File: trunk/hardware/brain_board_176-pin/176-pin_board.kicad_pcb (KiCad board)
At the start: 4 copper layers, 61.8 x 73.2 mm, 75 parts, among them J1 MINI-USB-5P-3400020P1, P1 CONN_25X2, P10 CONN_2X2, P11 CONN_4X2, P12 CONN_4X2, P2 CONN_25X2, P3 CONN_2, P4 CONN_6, P5 CONN_1, P6 CONN_2X2, P7 CONN_4X2, P8 CONN_4X2, P9 CONN_4X2, SW1 SW_PUSH, U1 STM32F407IGT6, U2 NUF2101MT1G, U3 LM2937, X1 CRYSTAL, X2 CRYSTAL

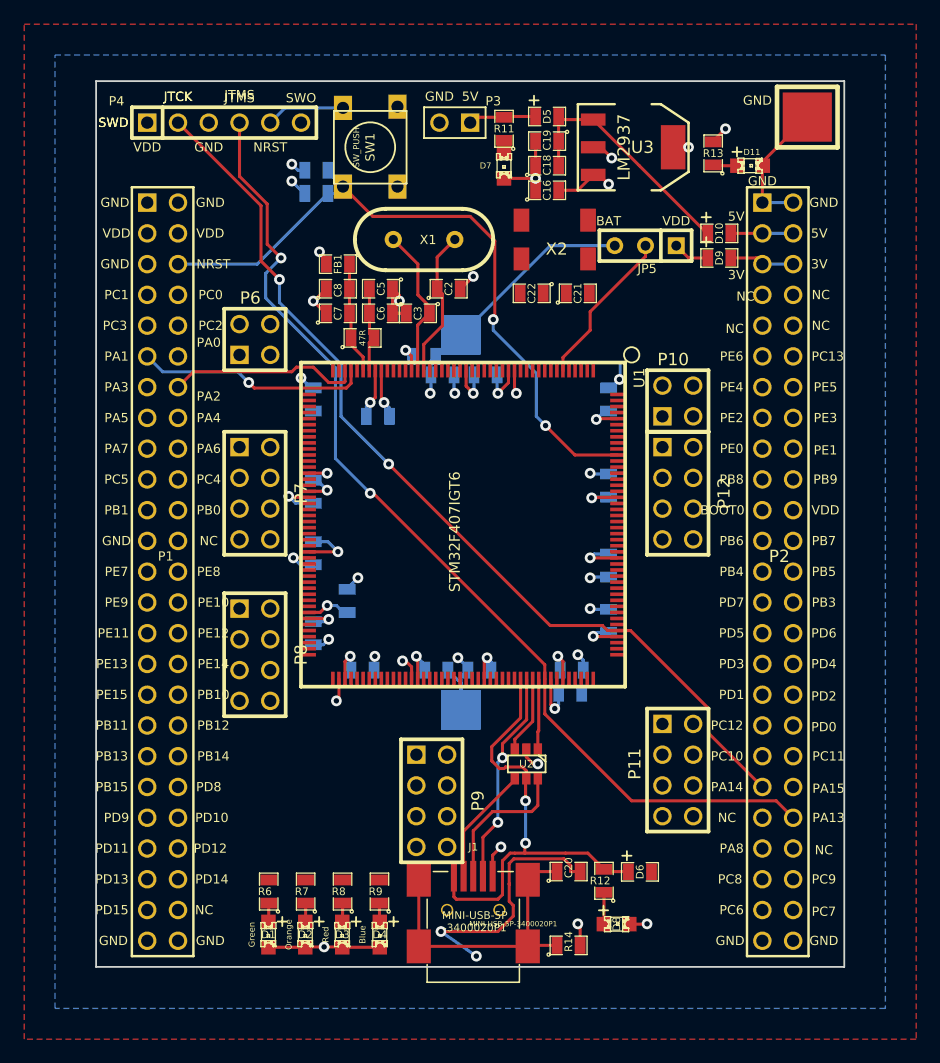
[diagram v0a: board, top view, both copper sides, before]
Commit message: 
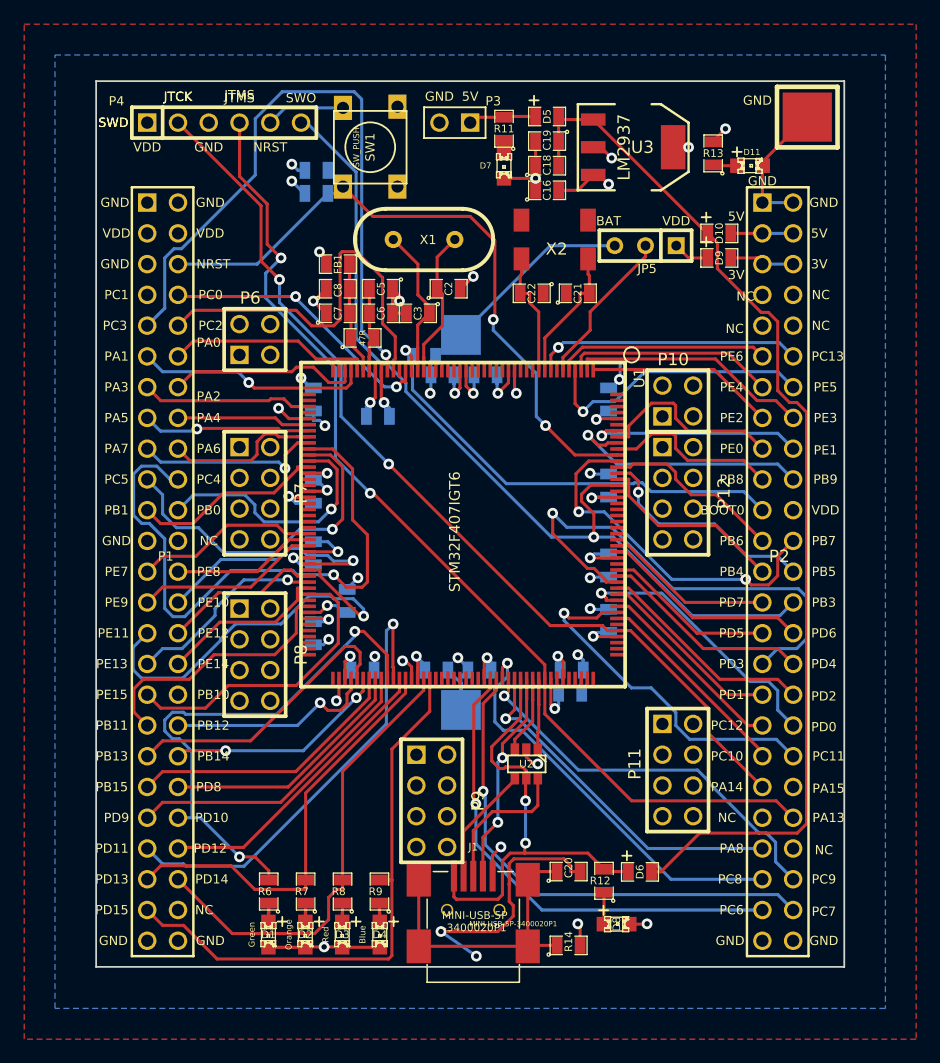
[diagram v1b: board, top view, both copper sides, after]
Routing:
- net /PB3: track 0.00 -> 73.6 mm, vias 0 -> 1
- net /5Vi: track 20.4 -> 88.7 mm
- net /PC3: track 0.00 -> 54.4 mm, vias 0 -> 1
- net /PC4: track 0.00 -> 50.4 mm, vias 0 -> 1
- net /PD15: track 0.00 -> 47.2 mm
- net /PD10: track 0.00 -> 44.0 mm, vias 0 -> 2
- net /PC7: track 0.00 -> 41.9 mm, vias 0 -> 1
- net /PD3: track 0.00 -> 40.6 mm, vias 0 -> 1
- net /PC6: track 0.00 -> 40.2 mm, vias 0 -> 1
- net /PD11: track 0.00 -> 38.3 mm, vias 0 -> 1
- net /PD14: track 0.00 -> 38.2 mm
- net /BOOT0: track 2.64 -> 39.1 mm
- net /PD13: track 0.00 -> 35.1 mm
- net /PC8: track 0.00 -> 34.2 mm, vias 0 -> 1
- net /PE11: track 0.00 -> 33.1 mm, vias 0 -> 1
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
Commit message: 
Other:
- net class Default: clearance 0.2032 -> 0.1524; trace_width 0.254 -> 0.1524
- rule trace_clearance: 0.2032 -> 0.1524
- rule trace_min: 0.254 -> 0.1524
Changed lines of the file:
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@@
   (general
     (links 250)
-    (no_connects 81)
+    (no_connects 8)
     (area 65.982549 61.494999 160.020001 171.672001)
     (thickness 1.6)
@@
   )
   (setup
-    (last_trace_width 0.254)
-    (trace_clearance 0.2032)
+    (last_trace_width 0.1524)
+    (trace_clearance 0.1524)
     (zone_clearance 0.254)
     (zone_45_only no)
-    (trace_min 0.254)
+    (trace_min 0.1524)
     (segment_width 0.2)
     (edge_width 0.15)
@@
   (net 105 N-0000078)
   (net_class Default "Это класс цепей по умолчанию."
-    (clearance 0.2032)
-    (trace_width 0.254)
+    (clearance 0.1524)
+    (trace_width 0.1524)
     (via_dia 0.889)
     (via_drill 0.635)

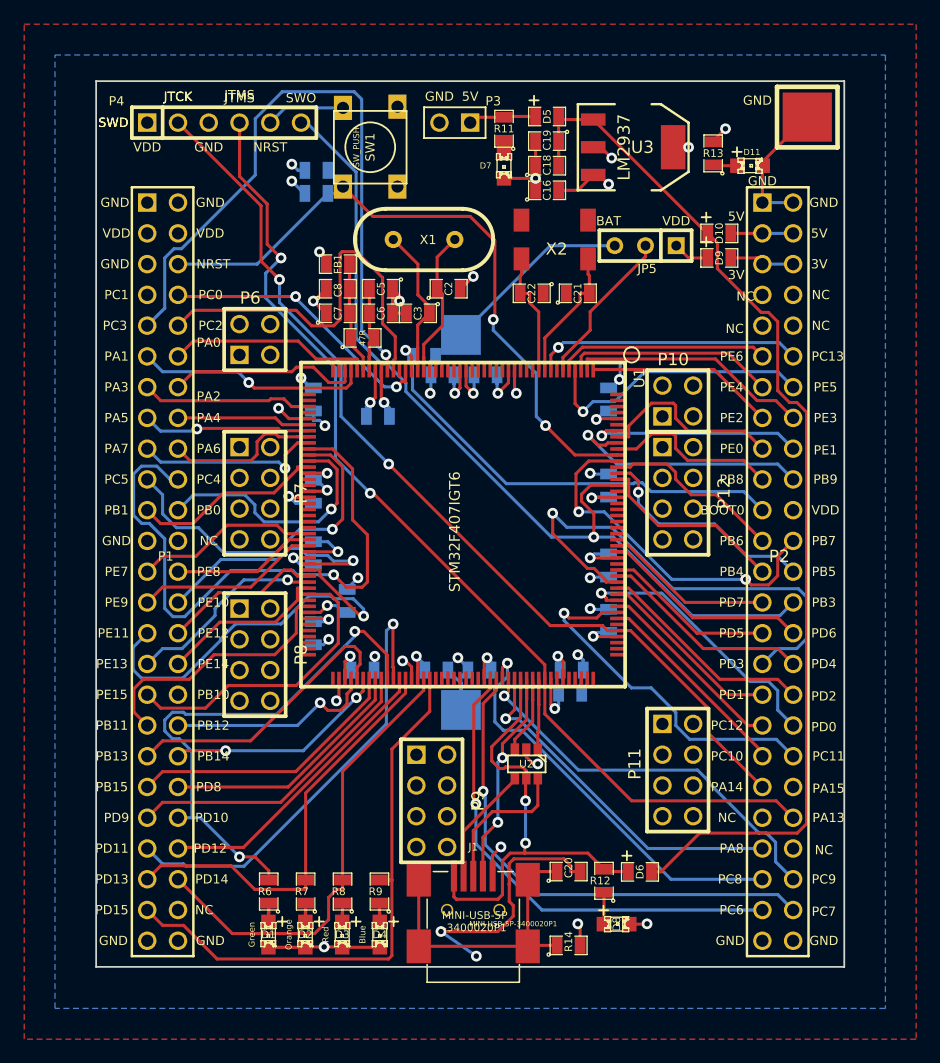
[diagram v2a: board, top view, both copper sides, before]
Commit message: 
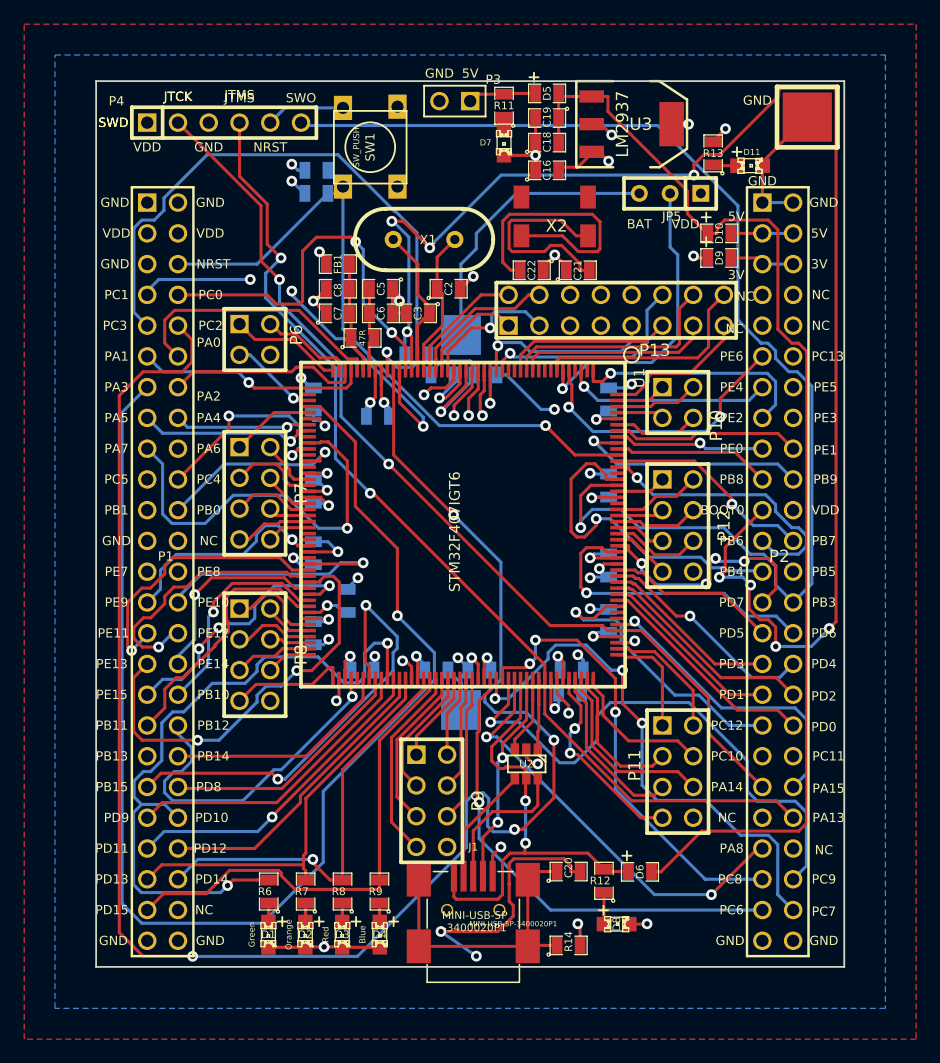
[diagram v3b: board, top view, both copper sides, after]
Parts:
- added P13: CONN_8X2, pin_array_8x2, F.Cu at (130.2, 102.4)
- moved JP5 4.77 mm to (134.6, 92.7)
- moved P12 2.67 mm to (135.3, 120.1)
- moved U3 1.91 mm to (131.4, 87.0)
- moved C18 1.91 mm to (124.5, 88.5)
- moved C19 1.91 mm to (124.5, 86.5)
- moved C21 1.91 mm to (127.0, 99.1)
- moved C22 1.91 mm to (123.2, 99.1)
- moved D5 1.91 mm to (124.5, 84.5)
- moved D7 1.91 mm to (120.9, 88.5)
- moved R11 1.91 mm to (120.9, 85.5)
- moved X2 1.91 mm to (125.1, 94.6)
- moved P3 1.78 mm to (116.8, 85.1)
- moved C16 1.65 mm to (124.5, 90.8)
- moved R4 0.65 mm to (113.7, 106.0)
- moved P10 0.13 mm to (135.3, 110.0), turned to 270 degrees
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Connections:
- P10 pad 1: (no net) -> /PI6
- P10 pad 2: (no net) -> /PI5
- P10 pad 3: (no net) -> /PI4
- P10 pad 4: (no net) -> /PDR_ON
- P11 pad 1: (no net) -> /PI2
- P11 pad 2: (no net) -> /PI3
- P11 pad 3: (no net) -> /PI0
- P11 pad 4: (no net) -> /PI1
- P11 pad 5: (no net) -> /PH14
- P11 pad 6: (no net) -> /PH15
- P11 pad 7: (no net) -> /PH13
- P11 pad 8: (no net) -> GND
- P12 pad 1: (no net) -> /PG15
- P12 pad 2: (no net) -> /PG14
- P12 pad 3: (no net) -> /PG13
- P12 pad 4: (no net) -> /PG12
- P12 pad 5: (no net) -> /PG11
- P12 pad 6: (no net) -> /PG10
- P12 pad 7: (no net) -> /PG9
- P12 pad 8: (no net) -> GND
- P6 pad 1: (no net) -> /PH3
- P6 pad 2: (no net) -> /PH2
- P6 pad 3: (no net) -> /PH5
- P6 pad 4: (no net) -> /PH4
- P7 pad 1: (no net) -> /BYPASS_REG
- P7 pad 2: (no net) -> /PF11
- P7 pad 3: (no net) -> /PF12
- P7 pad 4: (no net) -> /PF13
- P7 pad 5: (no net) -> /PF14
- P7 pad 6: (no net) -> /PF15
- P7 pad 7: (no net) -> /PG0
- P7 pad 8: (no net) -> /PG1
- P8 pad 1: (no net) -> /PH6
- P8 pad 2: (no net) -> /PH7
- P8 pad 3: (no net) -> /PH8
- P8 pad 4: (no net) -> /PH9
- P8 pad 5: (no net) -> /PH10
- P8 pad 6: (no net) -> /PH11
- P8 pad 7: (no net) -> /PH12
- P8 pad 8: (no net) -> GND
- P9 pad 1: (no net) -> /PG5
- P9 pad 2: (no net) -> /PG6
- P9 pad 3: (no net) -> /PG4
- P9 pad 4: (no net) -> /PG7
- P9 pad 5: (no net) -> /PG3
- P9 pad 6: (no net) -> /PG8
- P9 pad 7: (no net) -> /PG2
- P9 pad 8: (no net) -> GND
- U1 pad 106: (no net) -> /PG2
- U1 pad 107: (no net) -> /PG3
- U1 pad 108: (no net) -> /PG4
- U1 pad 109: (no net) -> /PG5
- U1 pad 11: (no net) -> /PI9
- U1 pad 110: (no net) -> /PG6
- U1 pad 111: (no net) -> /PG7
- U1 pad 112: (no net) -> /PG8
- U1 pad 12: (no net) -> /PI10
- U1 pad 128: (no net) -> /PH13
- U1 pad 129: (no net) -> /PH14
- U1 pad 13: (no net) -> /PI11
- U1 pad 130: (no net) -> /PH15
- U1 pad 131: (no net) -> /PI0
- U1 pad 132: (no net) -> /PI1
- U1 pad 133: (no net) -> /PI2
- U1 pad 134: (no net) -> /PI3
- U1 pad 152: (no net) -> /PG9
- U1 pad 153: (no net) -> /PG10
- U1 pad 154: (no net) -> /PG11
- U1 pad 155: (no net) -> /PG12
- U1 pad 156: (no net) -> /PG13
- U1 pad 157: (no net) -> /PG14
- U1 pad 16: (no net) -> /PF0
- U1 pad 160: (no net) -> /PG15
- U1 pad 17: (no net) -> /PF1
- U1 pad 171: (no net) -> /PDR_ON
- U1 pad 173: (no net) -> /PI4
- U1 pad 174: (no net) -> /PI5
- U1 pad 175: (no net) -> /PI6
- U1 pad 176: (no net) -> /PI7
- U1 pad 18: (no net) -> /PF2
- U1 pad 19: (no net) -> /PF3
- U1 pad 20: (no net) -> /PF4
- U1 pad 21: (no net) -> /PF5
- U1 pad 24: (no net) -> /PF6
- U1 pad 25: (no net) -> /PF7
- U1 pad 26: (no net) -> /PF8
- U1 pad 27: (no net) -> /PF9
- U1 pad 28: (no net) -> /PF10
- U1 pad 43: (no net) -> /PH2
- U1 pad 44: (no net) -> /PH3
- U1 pad 45: (no net) -> /PH4
- U1 pad 46: (no net) -> /PH5
- U1 pad 48: (no net) -> /BYPASS_REG
- U1 pad 59: (no net) -> /PF11
- U1 pad 60: (no net) -> /PF12
- U1 pad 63: (no net) -> /PF13
- U1 pad 64: (no net) -> /PF14
- U1 pad 65: (no net) -> /PF15
- U1 pad 66: (no net) -> /PG0
- U1 pad 67: (no net) -> /PG1
- U1 pad 7: (no net) -> /PI8
- U1 pad 83: (no net) -> /PH6
- U1 pad 84: (no net) -> /PH7
- U1 pad 85: (no net) -> /PH8
- U1 pad 86: (no net) -> /PH9
- U1 pad 87: (no net) -> /PH10
- U1 pad 88: (no net) -> /PH11
- U1 pad 89: (no net) -> /PH12
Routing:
- net /PC2: track 32.7 -> 146.9 mm, vias 0 -> 4
- net /PA3: track 14.1 -> 109.2 mm, vias 0 -> 1
- net /BOOT0: track 39.1 -> 125.8 mm, vias 1 -> 8
- net /PC1: track 0.00 -> 35.9 mm, vias 0 -> 3
- net /PC4: track 50.4 -> 17.5 mm, vias 1 -> 2
- net /PB3: track 73.6 -> 104.2 mm
- net /PF6: track 0.00 -> 29.6 mm, vias 0 -> 1
- net /PC11: track 29.6 -> 0.00 mm, vias 1 -> 0
- net /PC5: track 28.2 -> 0.00 mm, vias 1 -> 0
- net /PD3: track 40.6 -> 14.8 mm, vias 1 -> 0
- net /PA15: track 0.00 -> 25.2 mm, vias 0 -> 1
- net /PB13: track 23.8 -> 0.00 mm
- net /PE5: track 22.9 -> 0.00 mm, vias 1 -> 0
- net /PC13: track 22.2 -> 0.00 mm, vias 1 -> 0
- net /PF4: track 0.00 -> 21.9 mm, vias 0 -> 1
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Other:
- net class Default: clearance 0.1524 -> 0.2032; trace_width 0.1524 -> 0.254
- rule trace_clearance: 0.1524 -> 0.2032
- rule trace_min: 0.1524 -> 0.254

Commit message: 
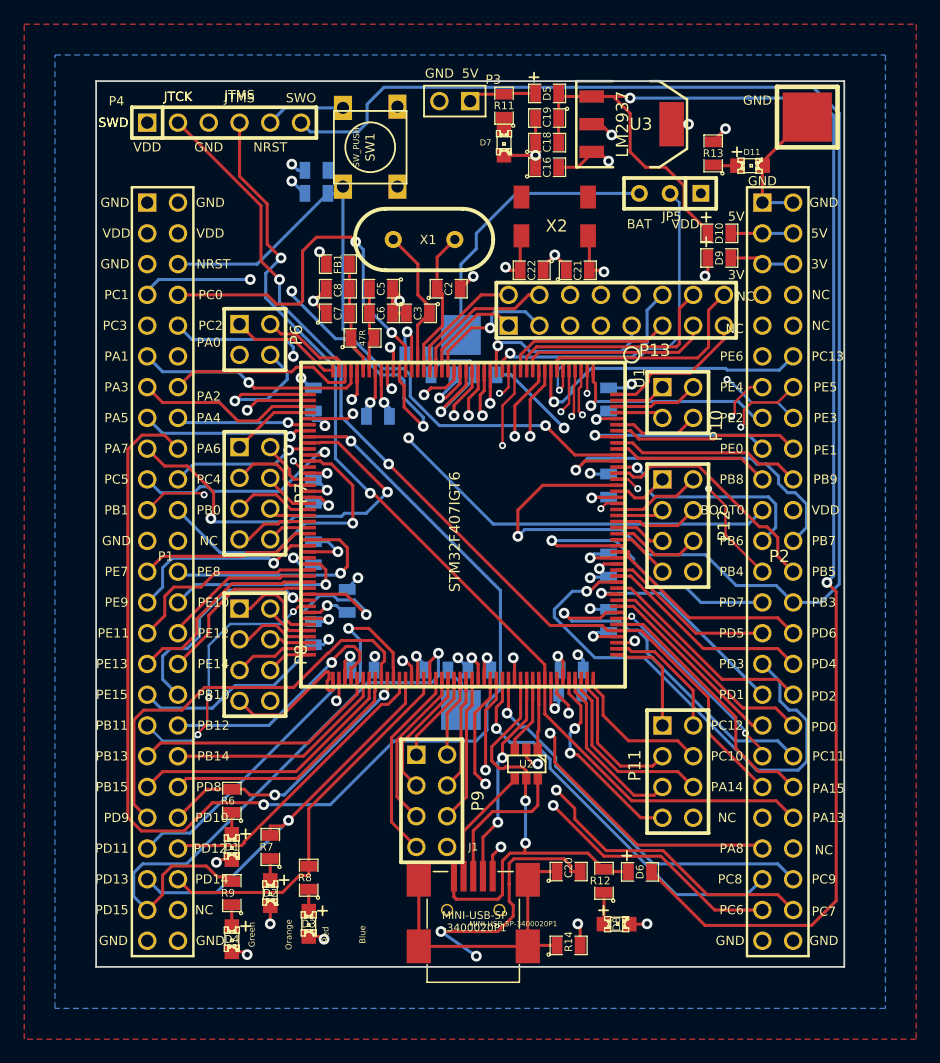
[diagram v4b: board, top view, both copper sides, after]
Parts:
- moved D4 12.2 mm to (98.4, 154.3)
- moved R9 12.2 mm to (98.4, 150.5)
- moved R6 8.09 mm to (98.4, 142.9)
- moved D1 7.84 mm to (98.4, 146.7)
- moved R7 4.70 mm to (101.6, 146.7)
- moved D2 4.49 mm to (101.6, 150.5)
- moved R8 3.02 mm to (104.8, 149.2)
- moved D3 2.91 mm to (104.8, 153.0)
- moved C16 0.25 mm to (124.5, 90.6)
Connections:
- net N-000008 renamed /VBAT
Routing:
- net /PC2: track 146.9 -> 22.8 mm, vias 4 -> 2
- net /PA6: track 0.00 -> 102.3 mm, vias 0 -> 2
- net /PA3: track 109.2 -> 15.0 mm, vias 1 -> 0
- net /BOOT0: track 125.8 -> 47.7 mm, vias 8 -> 2
- net /PD10: track 58.1 -> 23.0 mm
- net /5Vi: track 95.7 -> 128.3 mm, vias 0 -> 2
- net /PC11: track 0.00 -> 29.2 mm, vias 0 -> 1
- net /PC3: track 53.3 -> 24.9 mm
- net /PD3: track 14.8 -> 43.1 mm, vias 0 -> 1
- net /PE5: track 0.00 -> 27.8 mm, vias 0 -> 2
- net /PC13: track 0.00 -> 24.4 mm, vias 0 -> 1
- net /PB3: track 104.2 -> 128.1 mm
- net /PE3: track 0.00 -> 22.1 mm, vias 0 -> 2
- net /PB13: track 0.00 -> 20.7 mm
- net /PB5: track 0.00 -> 19.6 mm
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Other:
- net class smallest added: clearance 0.1778, trace_width 0.2032, via_dia 0.5842, via_drill 0.3302
- rule trace_min: 0.254 -> 0.2032
- rule via_min_drill: 0.508 -> 0.3302
- rule via_min_size: 0.889 -> 0.5588

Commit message: 
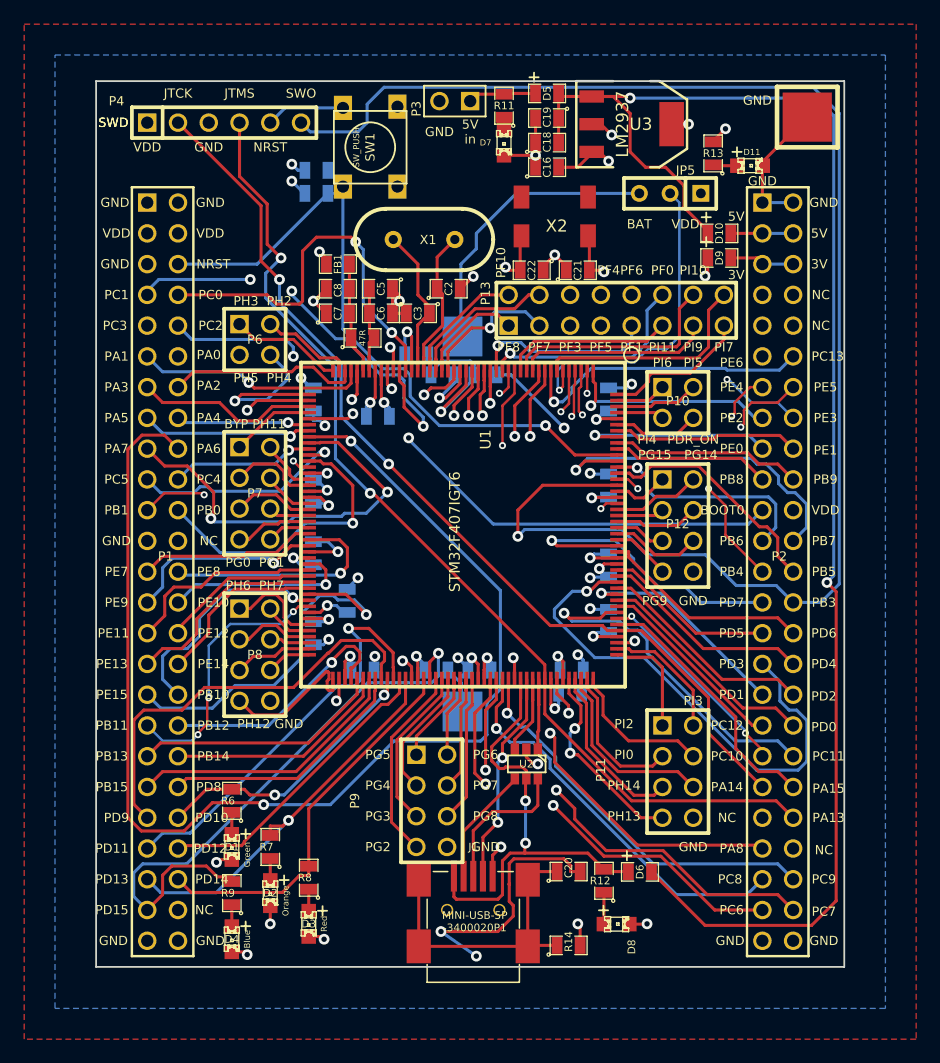
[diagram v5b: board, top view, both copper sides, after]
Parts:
- moved G1 11.4 mm to (105.4, 140.3)
- moved BT1 0.18 mm to (117.5, 120.0)
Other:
- board text added: "5V in"
- board text added: "BYP PH11"
- board text added: "PDR_ON"
- board text added: "PF0"
- board text added: "PF1"
- board text added: "PF10"
- board text added: "PF13 PF15"
- board text added: "PF2"
- board text added: "PF3"
- board text added: "PF4"
- board text added: "PF5"
- board text added: "PF6"
- board text added: "PF7"
- board text added: "PF8"
- board text added: "PF9"
- board text added: "PG0 PG1"
- board text added: "PG10"
- board text added: "PG13 PG11"
- board text added: "PG14"
- board text added: "PG15"
- board text added: "PG2"
- board text added: "PG3"
- board text added: "PG4"
- board text added: "PG5"
- board text added: "PG6"
- board text added: "PG7"
- board text added: "PG8"
- board text added: "PG9"
- board text added: "PH12 GND"
- board text added: "PH13"
- board text added: "PH14"
- board text added: "PH3 PH2"
- board text added: "PH5 PH4"
- board text added: "PH6 PH7"
- board text added: "PH9 PH11"
- board text added: "PI0"
- board text added: "PI1 PH15"
- board text added: "PI10"
- board text added: "PI11"
- board text added: "PI2"
- board text added: "PI3"
- board text added: "PI4"
- board text added: "PI5"
- board text added: "PI6"
- board text added: "PI7"
- board text added: "PI9"
- board text added: "STM VBAT"
